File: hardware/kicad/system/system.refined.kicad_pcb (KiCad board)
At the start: 2 copper layers, 203.1 x 152.4 mm, 131 parts, among them M501 IRF530, Q201 IRF540N, Q202 IRF530, Q401 IRF530, SW201 Switch, U201 LM7805, U202 MCP601, U203 NE555, U204 ILD74, U205 MCP601, U206 IR2110, U207 4N25, U208 IR2110, U301 MCP601, U302 IL300, U303 MCP601, U401 CNY17, U402 IR2110, U501 CNY17, U502 IR2110

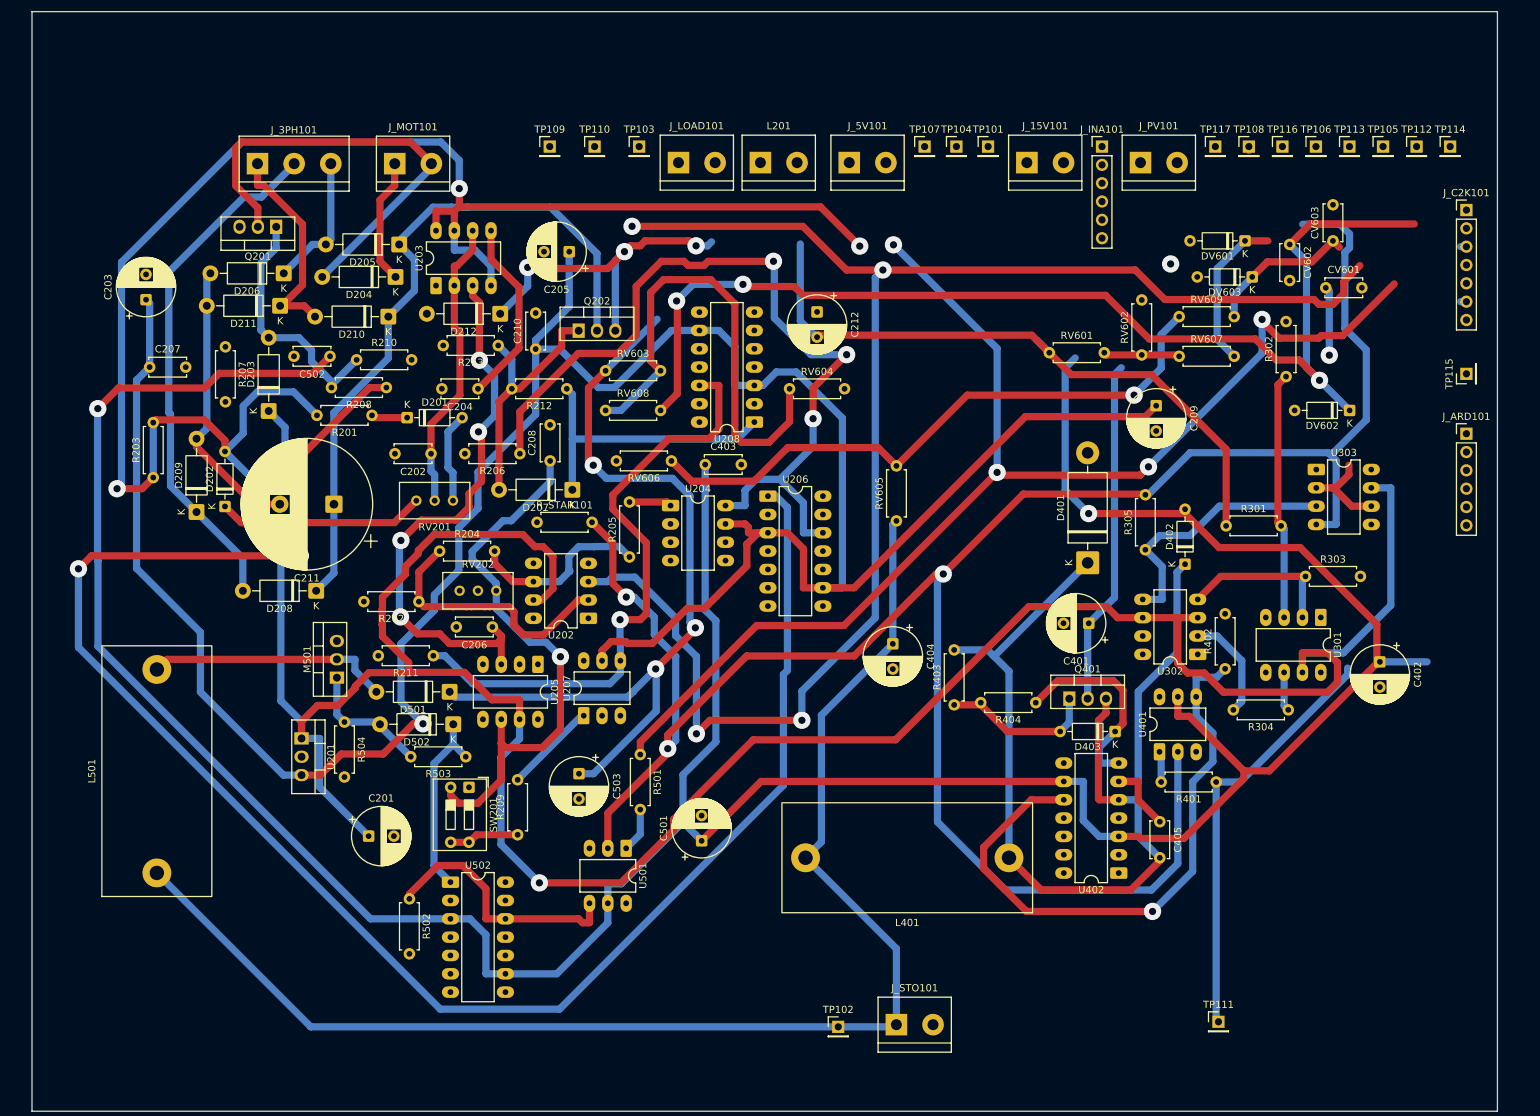
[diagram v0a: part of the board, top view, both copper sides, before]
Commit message: added system pcb layout
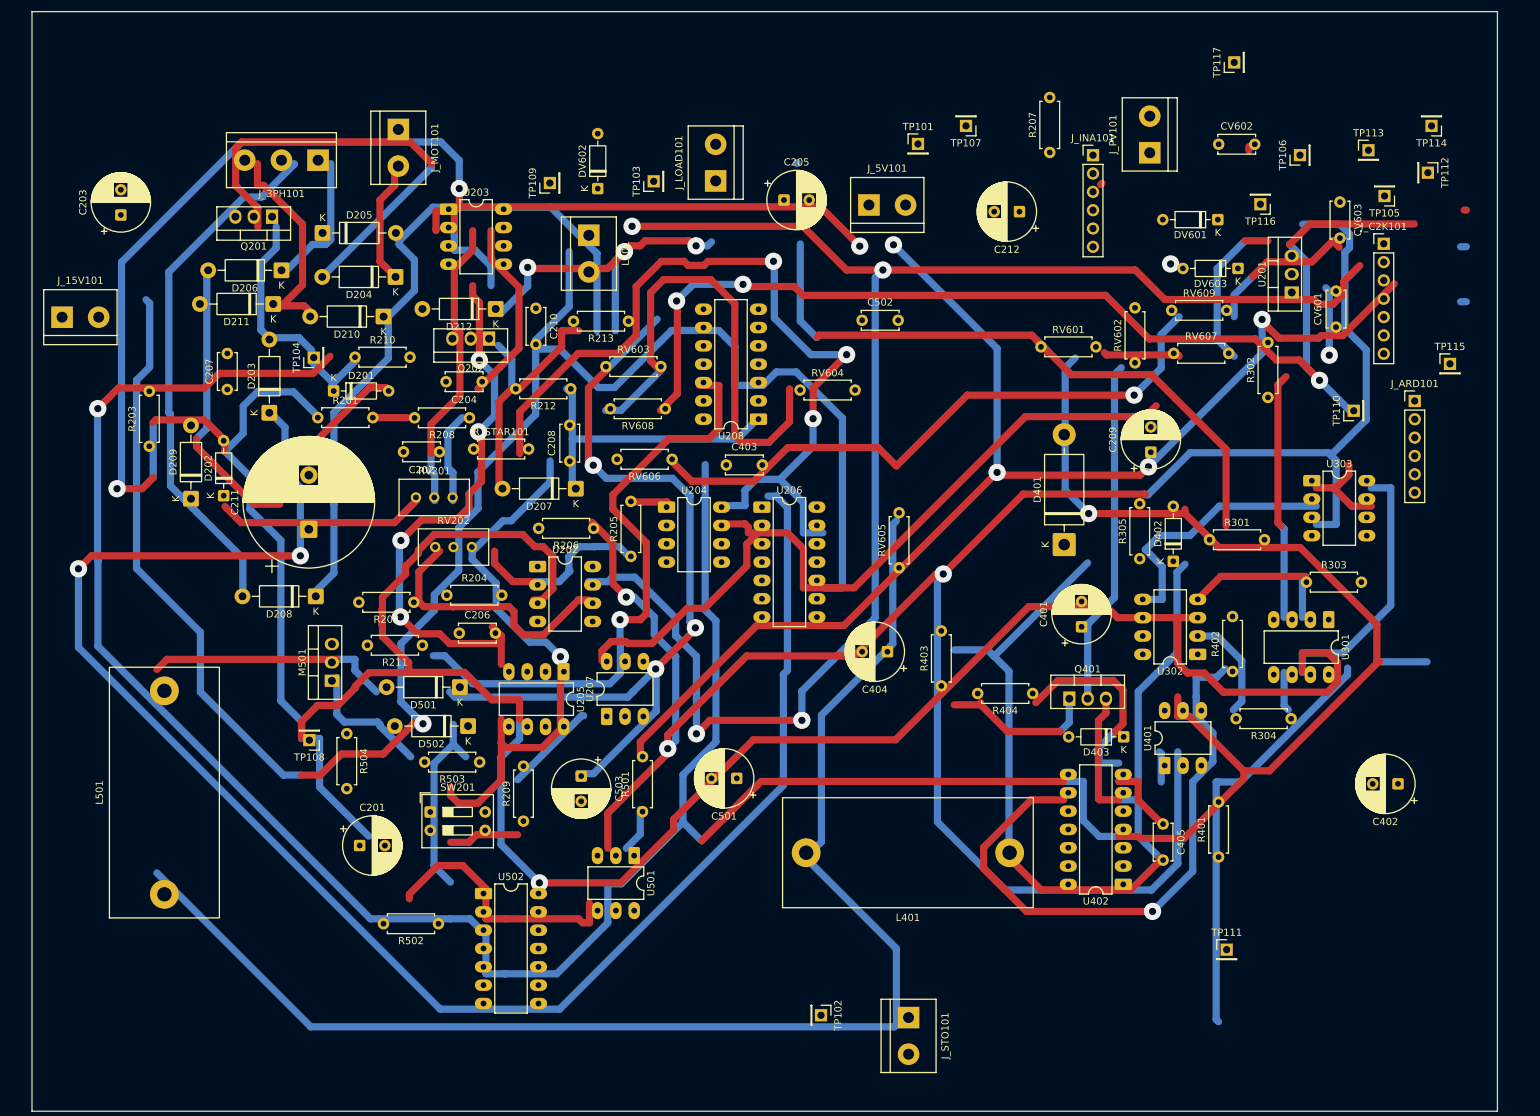
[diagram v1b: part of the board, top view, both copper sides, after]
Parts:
- moved TP108 154.0 mm to (137.4, 171.0), turned to 180 degrees
- moved U201 150.5 mm to (273.6, 108.9), turned to 90 degrees
- moved J_15V101 135.4 mm to (103.2, 112.3)
- moved R207 117.4 mm to (240.1, 89.5), turned to 90 degrees
- moved TP110 111.4 mm to (282.2, 125.3), turned to 90 degrees
- moved DV602 108.6 mm to (177.4, 94.5), turned to 90 degrees
- moved TP104 93.8 mm to (138.0, 118.0), turned to 90 degrees
- moved C502 73.9 mm to (214.0, 112.8), turned to 0 degrees
- moved C212 31.3 mm to (235.9, 97.7), turned to 180 degrees
- moved C205 30.6 mm to (203.2, 96.1), turned to 0 degrees
- moved L201 25.8 mm to (176.2, 101.0), turned to -90 degrees
- moved R213 18.4 mm to (181.7, 112.9)
- moved C402 17.1 mm to (288.3, 177.0), turned to 180 degrees
- moved CV602 17.0 mm to (263.5, 88.4), turned to 0 degrees
- moved R206 14.5 mm to (176.8, 141.6)
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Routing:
- net GND_MCU: track 308.2 -> 307.6 mm
- net GND: track 0.00 -> 0.56 mm
